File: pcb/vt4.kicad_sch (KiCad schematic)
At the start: 35 parts, among them J1 DE9, J2 DE9, J3 DE9, J4 DE9, J5 Mini-DIN-6, J7 USB_A, J8 USB_C_PowerOnly_6P, Q1 BSS138, Q2 BSS138, SW1 SW_SPDT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

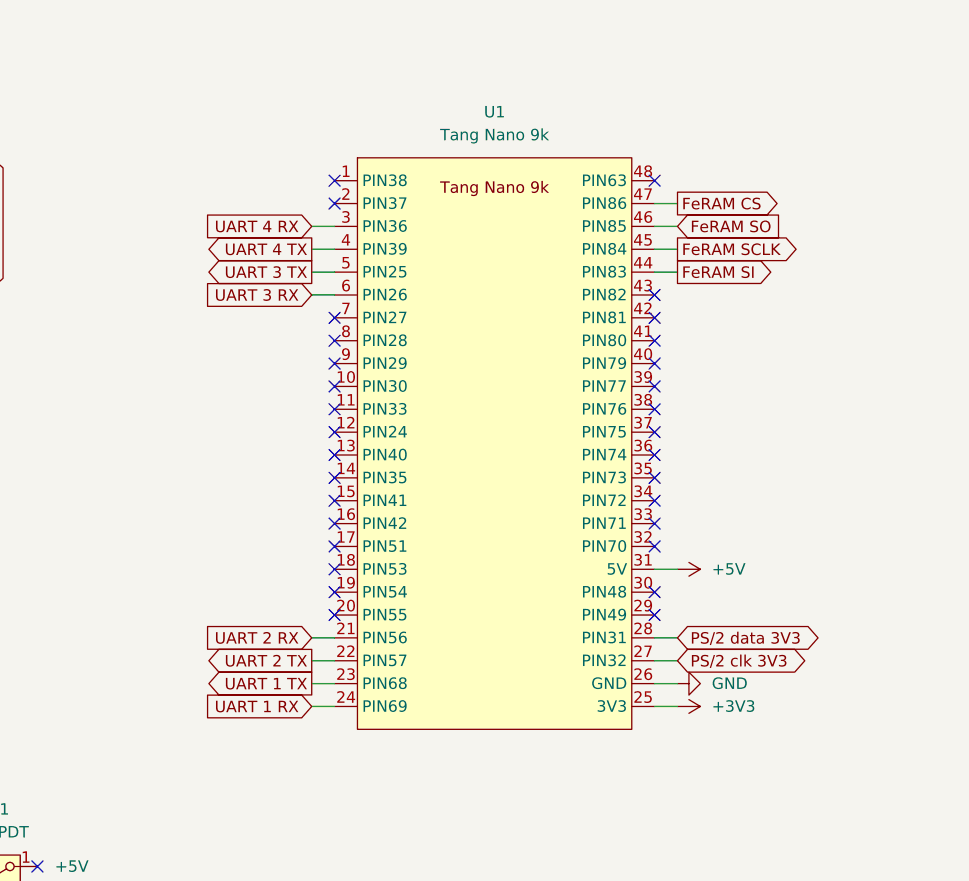
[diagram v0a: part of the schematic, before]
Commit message: PCB fail - connected UART 1 up to HDMI clk pins
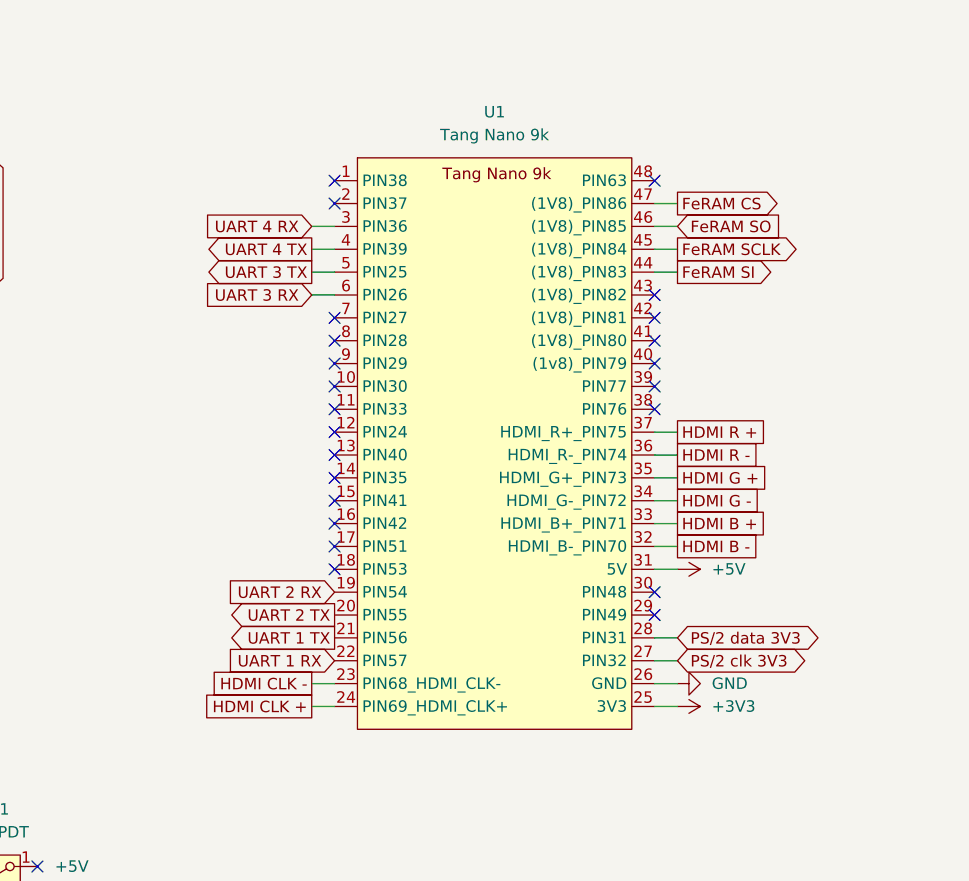
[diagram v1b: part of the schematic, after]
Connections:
- net UART 1 RX: now also U1.22 (PIN57); no longer U1.24 (PIN69)
- net UART 1 TX: now also U1.21 (PIN56); no longer U1.23 (PIN68)
- net UART 2 RX: now also U1.19 (PIN54); no longer U1.21 (PIN56)
- net UART 2 TX: now also U1.20 (PIN55); no longer U1.22 (PIN57)
- net HDMI B -: now reaches U1.32 (HDMI_B-_PIN70)
- net HDMI B +: now reaches U1.33 (HDMI_B+_PIN71)
- net HDMI G -: now reaches U1.34 (HDMI_G-_PIN72)
- net HDMI G +: now reaches U1.35 (HDMI_G+_PIN73)
- net HDMI R -: now reaches U1.36 (HDMI_R-_PIN74)
- net HDMI R +: now reaches U1.37 (HDMI_R+_PIN75)
- new net HDMI CLK +: U1.24 (PIN69_HDMI_CLK+)
- new net HDMI CLK -: U1.23 (PIN68_HDMI_CLK-)
- no-connect marks 66 -> 58

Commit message: Update PCB based on what was learnt soldering & testing
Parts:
- J1, J2, J3, J4: footprint 0-footprints:DSUB-9_Pins_Horizontal -> 0-footprints:DSUB_9_Pins_Female_Horizontal
- J8: footprint Connector_USB:USB_C_Receptacle_GCT_USB4125-xx-x-0190_6P_TopMnt_Horizontal -> 0-footprints:USB_C_Receptacle_GCT_USB4125-xx-x-0190_6P_TopMnt_Horizontal_Handsolder
- U2, U3: footprint Package_SO:SOIC-16_3.9x9.9mm_P1.27mm -> 0-footprints:SOIC-16_3.9x9.9mm_P1.27mm_Handsolder
- U4: footprint Package_SO:SOIC-8_5.3x5.3mm_P1.27mm -> 0-footprints:SOIC-8_5.3x5.3mm_P1.27mm_Handsolder
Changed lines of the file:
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@@
 			)
 		)
-		(property "Footprint" "0-footprints:DSUB-9_Pins_Horizontal"
+		(property "Footprint" "0-footprints:DSUB_9_Pins_Female_Horizontal"
 			(at 262.89 114.3 0)
 			(effects
@@
 			)
 		)
-		(property "Footprint" "Package_SO:SOIC-16_3.9x9.9mm_P1.27mm"
+		(property "Footprint" "0-footprints:SOIC-16_3.9x9.9mm_P1.27mm_Handsolder"
 			(at 205.74 158.75 0)
 			(effects
@@
 			)
 		)
-		(property "Footprint" "Package_SO:SOIC-16_3.9x9.9mm_P1.27mm"
+		(property "Footprint" "0-footprints:SOIC-16_3.9x9.9mm_P1.27mm_Handsolder"
 			(at 205.74 78.74 0)
 			(effects
@@
 			)
 		)
-		(property "Footprint" "0-footprints:DSUB-9_Pins_Horizontal"
+		(property "Footprint" "0-footprints:DSUB_9_Pins_Female_Horizontal"
 			(at 262.89 34.29 0)
 			(effects
@@
 			)
 		)
-		(property "Footprint" "Package_SO:SOIC-8_5.3x5.3mm_P1.27mm"
+		(property "Footprint" "0-footprints:SOIC-8_5.3x5.3mm_P1.27mm_Handsolder"
 			(at 102.87 29.21 0)
 			(effects
@@
 			)
 		)
-		(property "Footprint" "0-footprints:DSUB-9_Pins_Horizontal"
+		(property "Footprint" "0-footprints:DSUB_9_Pins_Female_Horizontal"
 			(at 262.89 149.86 0)
 			(effects
@@
 			)
 		)
-		(property "Footprint" "Connector_USB:USB_C_Receptacle_GCT_USB4125-xx-x-0190_6P_TopMnt_Horizontal"
+		(property "Footprint" "0-footprints:USB_C_Receptacle_GCT_USB4125-xx-x-0190_6P_TopMnt_Horizontal_Handsolder"
 			(at 40.64 152.4 0)
 			(effects
@@
 			)
 		)
-		(property "Footprint" "0-footprints:DSUB-9_Pins_Horizontal"
+		(property "Footprint" "0-footprints:DSUB_9_Pins_Female_Horizontal"
 			(at 262.89 69.85 0)
 			(effects

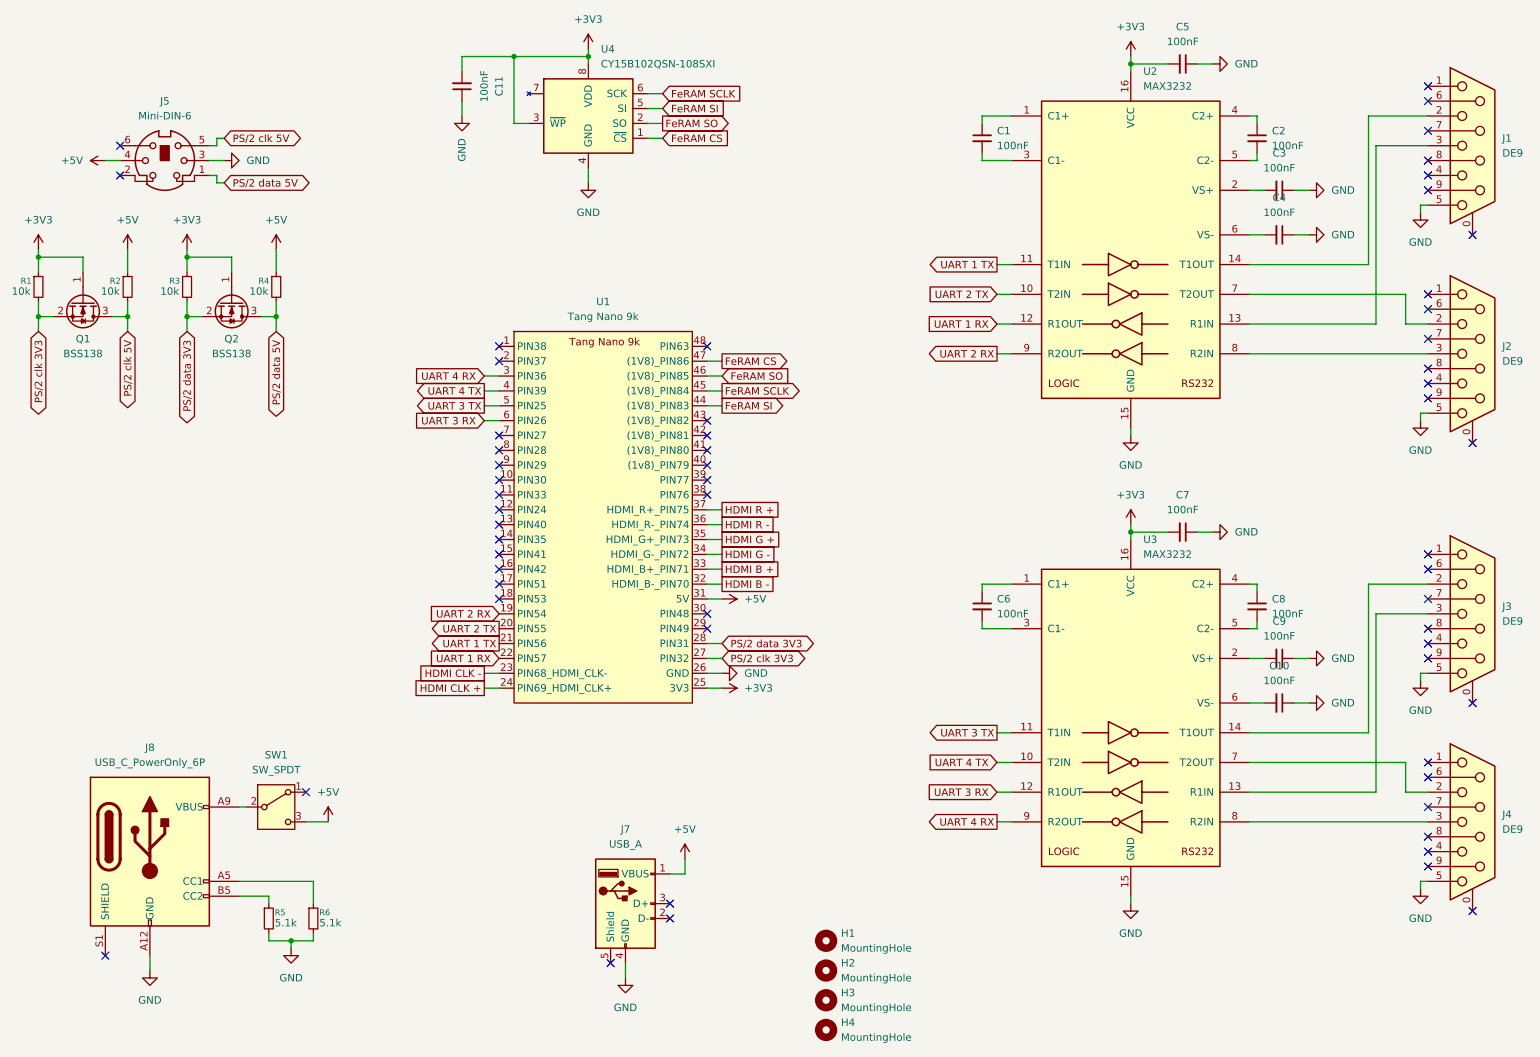
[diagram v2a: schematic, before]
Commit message: Send PCB of for manufacturing  * switch FeRAM to 3V3 pins (and supply)  * update FPGA pin numbers to match
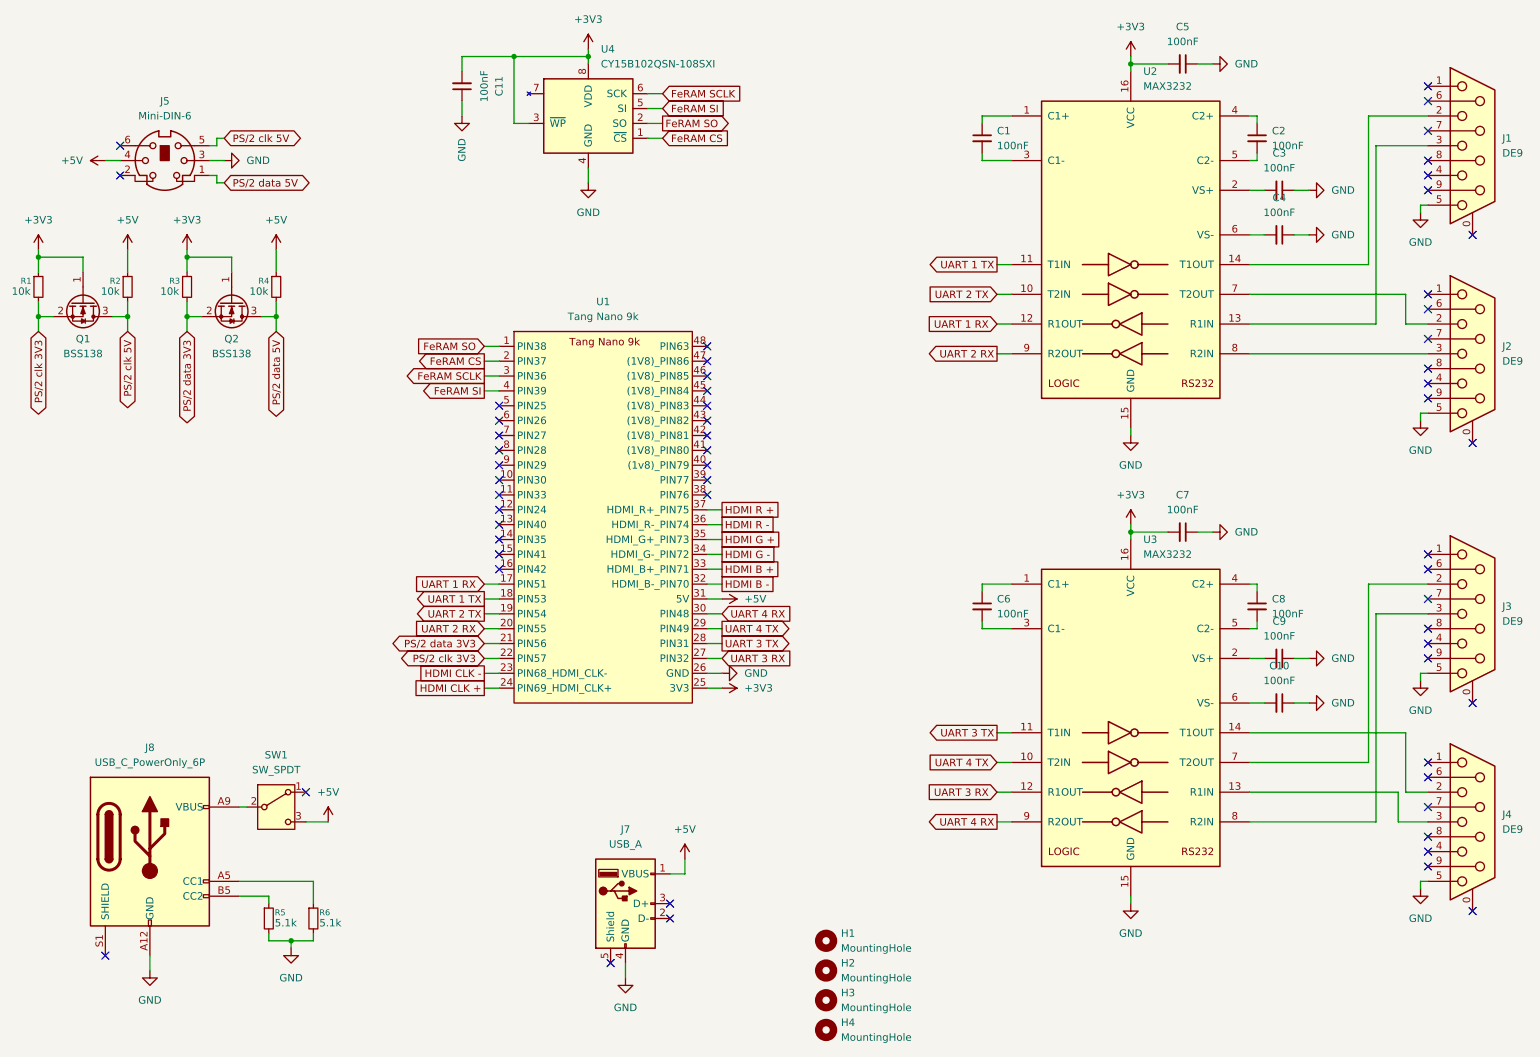
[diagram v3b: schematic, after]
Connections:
- net FeRAM CS: now also U1.2 (PIN37); no longer U1.47 ((1V8)_PIN86)
- net FeRAM SCLK: now also U1.3 (PIN36); no longer U1.45 ((1V8)_PIN84)
- net FeRAM SI: now also U1.4 (PIN39); no longer U1.44 ((1V8)_PIN83)
- net FeRAM SO: now also U1.1 (PIN38); no longer U1.46 ((1V8)_PIN85)
- net PS/2 clk 3V3: now also U1.22 (PIN57); no longer U1.27 (PIN32)
- net PS/2 data 3V3: now also U1.21 (PIN56); no longer U1.28 (PIN31)
- net UART 1 RX: now also U1.17 (PIN51); no longer U1.22 (PIN57)
- net UART 1 TX: now also U1.18 (PIN53); no longer U1.21 (PIN56)
- net UART 2 RX: now also U1.20 (PIN55); no longer U1.19 (PIN54)
- net UART 2 TX: now also U1.19 (PIN54); no longer U1.20 (PIN55)
- net UART 3 RX: now also U1.27 (PIN32); no longer U1.6 (PIN26)
- net UART 3 TX: now also U1.28 (PIN31); no longer U1.5 (PIN25)
- net UART 4 RX: now also U1.30 (PIN48); no longer U1.3 (PIN36)
- net UART 4 TX: now also U1.29 (PIN49); no longer U1.4 (PIN39)
- net at J3.2: now also U3.7 (T2OUT); no longer U3.14 (T1OUT)
- net at J3.3: now also U3.8 (R2IN); no longer U3.13 (R1IN)
- net at J4.2: now also U3.14 (T1OUT); no longer U3.7 (T2OUT)
- net at J4.3: now also U3.13 (R1IN); no longer U3.8 (R2IN)
